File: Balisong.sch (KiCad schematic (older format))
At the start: 14 parts

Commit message: The rest of the schematic
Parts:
- added D1, D2, D3, D4: D_Small, Diode_SMD:D_SOD-123, symbol Device:D_Small
- added F1: Polyfuse_Small, Fuse:Fuse_1206_3216Metric_Pad1.42x1.75mm_HandSolder, symbol Device:Polyfuse_Small
- added MX1, MX2, MX3, MX4: MX-NoLED, MX_Alps_Hybrid:MX-1U-NoLED, symbol MX_Alps_Hybrid:MX-NoLED
- added USB1: Molex-0548190589, random-keyboard-parts:Molex-0548190589, symbol random-keyboard-parts:Molex-0548190589
- C1, C2, C3, C4, C5, C6, C7: renamed from C?; footprint (none) -> Capacitor_SMD:C_0805_2012Metric
- R1: footprint (none) -> Resistor_SMD:R_0805_2012Metric
- R2, R3, R4: renamed from R?; footprint (none) -> Resistor_SMD:R_0805_2012Metric
- SW1: renamed from SW?; footprint (none) -> random-keyboard-parts:SKQG-1155865
- Y1: renamed from Y?; footprint (none) -> Crystal:Crystal_SMD_3225-4Pin_3.2x2.5mm
- gave numbers to parts that had none: 1
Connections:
- net +5V: now also F1.2
- net D+: now also USB1.3 (D+)
- net D-: now also USB1.4 (D-)
- net GND: now also USB1.1 (GND)
- new net: D3.2 (A), MX3.2 (ROW)
- new net: D1.2 (A), MX1.2 (ROW)
- new net: D2.2 (A), MX2.2 (ROW)
- new net: D4.2 (A), MX4.2 (ROW)
- new net COL0: MX1.1 (COL), MX2.1 (COL)
- new net COL1: MX3.1 (COL), MX4.1 (COL)
- new net ROW0: D1.1 (K), D3.1 (K)
- new net ROW1: D2.1 (K), D4.1 (K)
- new net VCC: F1.1, USB1.5 (VBUS)

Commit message: Creating the PCB
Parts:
- D1, D2, D3, D4: value D_Small -> SOD_123
- MX1, MX2, MX3, MX4: footprint MX_Alps_Hybrid:MX-1U-NoLED -> MX_Alps_Hybrid:MX-1U
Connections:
- net COL0: now also U1.29 (PB5)
- net COL1: now also U1.28 (PB4)
- net ROW0: now also U1.27 (PD7)
- net ROW1: now also U1.30 (PB6)
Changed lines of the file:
@@
 F 0 "MX3" H 7933 1773 60  0000 C CNN
 F 1 "MX-NoLED" H 7933 1699 20  0000 C CNN
-F 2 "MX_Alps_Hybrid:MX-1U-NoLED" H 7275 1525 60  0001 C CNN
+F 2 "MX_Alps_Hybrid:MX-1U" H 7275 1525 60  0001 C CNN
 F 3 "" H 7275 1525 60  0001 C CNN
 	1    7900 1550
@@
 F 0 "MX1" H 7483 1773 60  0000 C CNN
 F 1 "MX-NoLED" H 7483 1699 20  0000 C CNN
-F 2 "MX_Alps_Hybrid:MX-1U-NoLED" H 6825 1525 60  0001 C CNN
+F 2 "MX_Alps_Hybrid:MX-1U" H 6825 1525 60  0001 C CNN
 F 3 "" H 6825 1525 60  0001 C CNN
 	1    7450 1550
@@
 F 0 "MX2" H 7483 2423 60  0000 C CNN
 F 1 "MX-NoLED" H 7483 2349 20  0000 C CNN
-F 2 "MX_Alps_Hybrid:MX-1U-NoLED" H 6825 2175 60  0001 C CNN
+F 2 "MX_Alps_Hybrid:MX-1U" H 6825 2175 60  0001 C CNN
 F 3 "" H 6825 2175 60  0001 C CNN
 	1    7450 2200
@@
 F 0 "MX4" H 7933 2423 60  0000 C CNN
 F 1 "MX-NoLED" H 7933 2349 20  0000 C CNN
-F 2 "MX_Alps_Hybrid:MX-1U-NoLED" H 7275 2175 60  0001 C CNN
+F 2 "MX_Alps_Hybrid:MX-1U" H 7275 2175 60  0001 C CNN
 F 3 "" H 7275 2175 60  0001 C CNN
 	1    7900 2200
@@
 P 7400 2450
 F 0 "D2" V 7446 2382 50  0000 R CNN
-F 1 "D_Small" V 7355 2382 50  0000 R CNN
+F 1 "SOD_123" V 7355 2382 50  0000 R CNN
 F 2 "Diode_SMD:D_SOD-123" V 7400 2450 50  0001 C CNN
 F 3 "~" V 7400 2450 50  0001 C CNN
@@
 P 7850 2450
 F 0 "D4" V 7896 2382 50  0000 R CNN
-F 1 "D_Small" V 7805 2382 50  0000 R CNN
+F 1 "SOD_123" V 7805 2382 50  0000 R CNN
 F 2 "Diode_SMD:D_SOD-123" V 7850 2450 50  0001 C CNN
 F 3 "~" V 7850 2450 50  0001 C CNN
@@
 P 7400 1800
 F 0 "D1" V 7446 1732 50  0000 R CNN
-F 1 "D_Small" V 7355 1732 50  0000 R CNN
+F 1 "SOD_123" V 7355 1732 50  0000 R CNN
 F 2 "Diode_SMD:D_SOD-123" V 7400 1800 50  0001 C CNN
 F 3 "~" V 7400 1800 50  0001 C CNN
@@
 P 7850 1800
 F 0 "D3" V 7896 1732 50  0000 R CNN
-F 1 "D_Small" V 7805 1732 50  0000 R CNN
+F 1 "SOD_123" V 7805 1732 50  0000 R CNN
 F 2 "Diode_SMD:D_SOD-123" V 7850 1800 50  0001 C CNN
 F 3 "~" V 7850 1800 50  0001 C CNN
@@
 Text GLabel 8050 1100 1    50   Input ~ 0
 COL1
+Text GLabel 4450 3500 2    50   Input ~ 0
+ROW0
+Text GLabel 4450 2000 2    50   Input ~ 0
+COL1
+Text GLabel 4450 2100 2    50   Input ~ 0
+COL0
+Text GLabel 4450 2200 2    50   Input ~ 0
+ROW1
 $EndSCHEMATC

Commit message: Creating the gerber
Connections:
- no-connect marks 0 -> 1
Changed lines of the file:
@@
 Text GLabel 4450 2200 2    50   Input ~ 0
 ROW1
+NoConn ~ 5600 1250
 $EndSCHEMATC

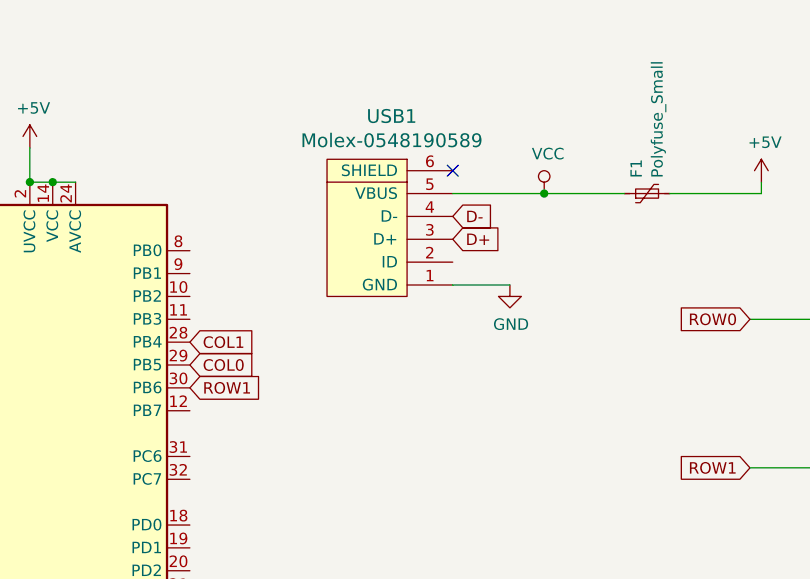
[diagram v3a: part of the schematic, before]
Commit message: Changed USB connectors
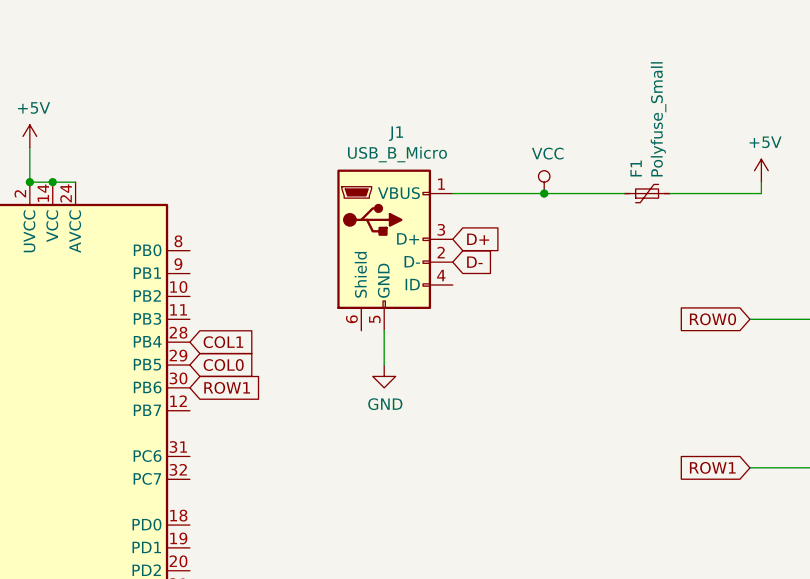
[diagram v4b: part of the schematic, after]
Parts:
- removed USB1: Molex-0548190589, random-keyboard-parts:Molex-0548190589, symbol random-keyboard-parts:Molex-0548190589
- added J1: USB_B_Micro, Connector_USB:USB_Micro-B_Molex_47346-0001, symbol Connector:USB_B_Micro
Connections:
- net D+: now also J1.3 (D+)
- net D-: now also J1.2 (D-)
- net GND: now also J1.5 (GND)
- net VCC: now also J1.1 (VBUS)
- no-connect marks 1 -> 0
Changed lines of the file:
@@
 D-
-$Comp
-L random-keyboard-parts:Molex-0548190589 USB1
-U 1 1 5EBB7931
-P 5300 1550
-F 0 "USB1" V 5837 1517 60  0000 C CNN
-F 1 "Molex-0548190589" V 5731 1517 60  0000 C CNN
-F 2 "random-keyboard-parts:Molex-0548190589" H 5300 1550 60  0001 C CNN
-F 3 "" H 5300 1550 60  0001 C CNN
-	1    5300 1550
-	0    -1   -1   0
-$EndComp
 $Comp
 L Device:Polyfuse_Small F1
@@
 L power:GND #PWR0113
 U 1 1 5EBCD310
-P 5850 1750
-F 0 "#PWR0113" H 5850 1500 50  0001 C CNN
-F 1 "GND" H 5855 1577 50  0000 C CNN
-F 2 "" H 5850 1750 50  0001 C CNN
-F 3 "" H 5850 1750 50  0001 C CNN
-	1    5850 1750
+P 5300 2100
+F 0 "#PWR0113" H 5300 1850 50  0001 C CNN
+F 1 "GND" H 5305 1927 50  0000 C CNN
+F 2 "" H 5300 2100 50  0001 C CNN
+F 3 "" H 5300 2100 50  0001 C CNN
+	1    5300 2100
 	1    0    0    -1
 $EndComp
-Wire Wire Line
-	5600 1750 5850 1750
 Text GLabel 5600 1550 2    50   Input ~ 0
 D+
-Text GLabel 5600 1450 2    50   Input ~ 0
+Text GLabel 5600 1650 2    50   Input ~ 0
 D-
 $Comp
@@
 Text GLabel 4450 2200 2    50   Input ~ 0
 ROW1
-NoConn ~ 5600 1250
+$Comp
+L Connector:USB_B_Micro J1
+U 1 1 5EBC7237
+P 5300 1550
+F 0 "J1" H 5357 2017 50  0000 C CNN
+F 1 "USB_B_Micro" H 5357 1926 50  0000 C CNN
+F 2 "Connector_USB:USB_Micro-B_Molex_47346-0001" H 5450 1500 50  0001 C CNN
+F 3 "~" H 5450 1500 50  0001 C CNN
+	1    5300 1550
+	1    0    0    -1
+$EndComp
+Wire Wire Line
+	5300 1950 5300 2100
 $EndSCHEMATC

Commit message: Update
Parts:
- removed D1, D3, D4: SOD_123, Diode_SMD:D_SOD-123, symbol Device:D_Small
- removed MX1, MX2, MX3, MX4: MX-NoLED, MX_Alps_Hybrid:MX-1U, symbol MX_Alps_Hybrid:MX-NoLED
- removed SW1: SW_Push, random-keyboard-parts:SKQG-1155865, symbol Switch:SW_Push
- added D? (x51): SOD_123, Diode_SMD:D_SOD-123, symbol Device:D_Small
- added SW? (x52): MX, symbol Switch:SW_Push
- F1: footprint Fuse:Fuse_1206_3216Metric_Pad1.42x1.75mm_HandSolder -> Fuse:Fuse_1206_3216Metric_Castellated
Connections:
- net COL0: now also SW?.2, SW?.2, SW?.2, SW?.2
- net COL1: now also SW?.2, SW?.2, SW?.2, SW?.2
- net ROW0: now also D?.1 (K), D?.1 (K), D?.1 (K), D?.1 (K), D?.1 (K), D?.1 (K), D?.1 (K), D?.1 (K), D?.1 (K), D?.1 (K), D?.1 (K), D?.1 (K), D?.1 (K), D?.1 (K)
- net ROW1: now also D?.1 (K), D?.1 (K), D?.1 (K), D?.1 (K), D?.1 (K), D?.1 (K), D?.1 (K), D?.1 (K), D?.1 (K), D?.1 (K), D?.1 (K), D?.1 (K), D?.1 (K)
- net at D2.2 (A): now also SW?.1
- new net: D?.2 (A), SW?.1 (x51)
- new net COL10: SW?.2, SW?.2, SW?.2
- new net COL11: SW?.2, SW?.2, SW?.2, SW?.2
- new net COL12: SW?.2, SW?.2, SW?.2, SW?.2
- new net COL13: SW?.2, SW?.2, SW?.2, SW?.2
- new net COL2: SW?.2, SW?.2, SW?.2, SW?.2
- new net COL3: SW?.2, SW?.2, SW?.2
- new net COL4: SW?.2, SW?.2, SW?.2, SW?.2
- new net COL5: SW?.2, SW?.2, SW?.2
- new net COL6: SW?.2, SW?.2, SW?.2, SW?.2
- new net COL7: SW?.2, SW?.2, SW?.2, SW?.2
- new net COL8: SW?.2, SW?.2, SW?.2
- new net COL9: SW?.2, SW?.2, SW?.2, SW?.2
- new net ROW2: D?.1 (K), D?.1 (K), D?.1 (K), D?.1 (K), D?.1 (K), D?.1 (K), D?.1 (K), D?.1 (K), D?.1 (K), D?.1 (K), D?.1 (K), D?.1 (K), D?.1 (K), D?.1 (K)
- new net ROW3: D?.1 (K), D?.1 (K), D?.1 (K), D?.1 (K), D?.1 (K), D?.1 (K), D?.1 (K), D?.1 (K), D?.1 (K), D?.1 (K)
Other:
- moved on the sheet: D2

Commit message: Finished pcb
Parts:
- removed C3: 0.1uF, Capacitor_SMD:C_0805_2012Metric, symbol Device:C_Small
- removed F1: Polyfuse_Small, Fuse:Fuse_1206_3216Metric_Castellated, symbol Device:Polyfuse_Small
- removed Y1: 16MHz, Crystal:Crystal_SMD_3225-4Pin_3.2x2.5mm, symbol Device:Crystal_GND24_Small
- added C1: 0.1uF, Capacitor_SMD:C_0805_2012Metric_Pad1.15x1.40mm_HandSolder, symbol Device:C_Small
- added SW53: SW_Push, Button_Switch_SMD:SW_SPST_B3U-1000P, symbol Switch:SW_Push
- added Y1: 16MHz, Crystal:Crystal_SMD_Abracon_ABM3-2Pin_5.0x3.2mm_HandSoldering, symbol Device:Crystal_Small
- C2: renamed from C1; footprint Capacitor_SMD:C_0805_2012Metric -> Capacitor_SMD:C_0805_2012Metric_Pad1.15x1.40mm_HandSolder
- C3: renamed from C2; footprint Capacitor_SMD:C_0805_2012Metric -> Capacitor_SMD:C_0805_2012Metric_Pad1.15x1.40mm_HandSolder
- C5: renamed from C7; footprint Capacitor_SMD:C_0805_2012Metric -> Capacitor_SMD:C_0805_2012Metric_Pad1.15x1.40mm_HandSolder
- C6: footprint Capacitor_SMD:C_0805_2012Metric -> Capacitor_SMD:C_0805_2012Metric_Pad1.15x1.40mm_HandSolder
- C7: renamed from C4; footprint Capacitor_SMD:C_0805_2012Metric -> Capacitor_SMD:C_0805_2012Metric_Pad1.15x1.40mm_HandSolder
- C8: renamed from C5; footprint Capacitor_SMD:C_0805_2012Metric -> Capacitor_SMD:C_0805_2012Metric_Pad1.15x1.40mm_HandSolder
- R1, R3: footprint Resistor_SMD:R_0805_2012Metric -> Resistor_SMD:R_0805_2012Metric_Pad1.15x1.40mm_HandSolder
- R2: renamed from R4; footprint Resistor_SMD:R_0805_2012Metric -> Resistor_SMD:R_0805_2012Metric_Pad1.15x1.40mm_HandSolder
- R4: renamed from R2; footprint Resistor_SMD:R_0805_2012Metric -> Resistor_SMD:R_0805_2012Metric_Pad1.15x1.40mm_HandSolder
- SW1, SW25, SW29, SW49: renamed from SW?; footprint (none) -> Button_Switch_Keyboard:SW_Cherry_MX_1.50u_PCB
- SW10, SW11, SW13, SW14, SW15, SW16, SW17, SW18, SW20, SW21, SW22, SW23, SW26, SW27, SW3, SW30, SW31, SW32, SW33, SW34, SW35, SW36, SW38, SW39, SW40, SW41, SW42, SW43, SW45, SW46, SW47, SW5, SW51, SW6, SW7, SW9: renamed from SW?; footprint (none) -> Button_Switch_Keyboard:SW_Cherry_MX_1.00u_PCB
- SW12, SW2, SW24, SW28, SW4, SW44, SW48, SW50, SW52, SW8: renamed from SW?; footprint (none) -> Button_Switch_Keyboard:SW_Cherry_MX_1.25u_PCB
- SW19, SW37: renamed from SW?; footprint (none) -> Button_Switch_Keyboard:SW_Cherry_MX_2.75u_PCB
- gave numbers to parts that had none: 51
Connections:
- net labels removed: +5V
- wire segments 199 -> 193
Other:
- moved on the sheet: C2, C3, C6, J1, R3, R4
